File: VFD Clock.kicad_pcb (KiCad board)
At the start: 2 copper layers, 224 x 78.5 mm, 37 parts, among them J2 Mode Button, J3 Up Button, J4 Down Button, J5 Select Button, U1 74HC595, U10 74HC595, U11 UDN2981A, U12 Minute Right, U13 74HC595, U14 UDN2981A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

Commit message: removed all tracks, starting over
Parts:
- moved J5 51.0 mm to (275.5, 143.0)
- moved J4 48.0 mm to (261.5, 143.0)
- moved J3 44.0 mm to (247.5, 143.0)
- moved U21 43.1 mm to (225.4, 126.1)
- moved J2 41.0 mm to (233.5, 143.0)
- moved C10 24.0 mm to (88.5, 119.0)
- moved C1 6.52 mm to (76.0, 92.0)
- moved U13 4.00 mm to (215.5, 114.0)
- moved U5 4.00 mm to (137.5, 84.0)
- moved C8 3.03 mm to (151.0, 119.0)
- moved U7 3.03 mm to (153.5, 114.0)
- moved U4 3.01 mm to (118.5, 114.0)
- moved C9 3.00 mm to (115.0, 119.0)
- moved C7 1.00 mm to (177.0, 119.0)
- moved U10 1.00 mm to (180.5, 114.0)
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- renumbered REF** to Hole1, REF** to Hole2, REF** to Hole3, REF** to Hole4
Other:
- board size 224 x 78.5 mm -> 224 x 78 mm
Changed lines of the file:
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@@
 	(footprint "MountingHole:MountingHole_3.2mm_M3"
 		(layer "F.Cu")
-		(at 66.881135 74.954983)
+		(at 67 75.5)
 		(descr "Mounting Hole 3.2mm, M3, no annular, generated by kicad-footprint-generator mountinghole.py")
 		(tags "mountinghole M3")
-		(property "Reference" "REF**"
+		(property "Reference" "Hole1"
 			(at 0 -4.15 0)
 			(layer "F.SilkS")
@@
 			(layer "F.CrtYd")
 		)
-		(fp_text user "${REFERENCE}"
+		(fp_text user "$Hole1"
 			(at 0 0 0)
 			(layer "F.Fab")
@@
 		(descr "Mounting Hole 3.2mm, M3, no annular, generated by kicad-footprint-generator mountinghole.py")
 		(tags "mountinghole M3")
-		(property "Reference" "REF**"
+		(property "Reference" "Hole4"
 			(at 0 -4.15 0)
 			(layer "F.SilkS")
@@
 			(layer "F.CrtYd")
 		)
-		(fp_text user "${REFERENCE}"
+		(fp_text user "$Hole4"
 			(at 0 0 0)
 			(layer "F.Fab")
@@
 	(footprint "MountingHole:MountingHole_3.2mm_M3"
 		(layer "F.Cu")
-		(at 66.945211 146.450088)
+		(at 67 146.5)
 		(descr "Mounting Hole 3.2mm, M3, no annular, generated by kicad-footprint-generator mountinghole.py")
 		(tags "mountinghole M3")
-		(property "Reference" "REF**"
+		(property "Reference" "Hole2"
 			(at 0 -4.15 0)
 			(layer "F.SilkS")
@@
 			(layer "F.CrtYd")
 		)
-		(fp_text user "${REFERENCE}"
+		(fp_text user "$Hole2"
 			(at 0 0 0)
 			(layer "F.Fab")
@@
 	(footprint "MountingHole:MountingHole_3.2mm_M3"
 		(layer "F.Cu")
-		(at 284 75)
+		(at 284 75.5)
 		(descr "Mounting Hole 3.2mm, M3, no annular, generated by kicad-footprint-generator mountinghole.py")
 		(tags "mountinghole M3")
-		(property "Reference" "REF**"
+		(property "Reference" "Hole3"
 			(at 0 -4.15 0)
 			(layer "F.SilkS")
@@
 			(layer "F.CrtYd")
 		)
-		(fp_text user "${REFERENCE}"
+		(fp_text user "$Hole3"
 			(at 0 0 0)
 			(layer "F.Fab")
@@
 	(footprint "Custom Parts:DS3231 Module"
 		(layer "B.Cu")
-		(at 268.5 126 180)
+		(at 225.4 126.1 180)
 		(property "Reference" "U21"
 			(at 22 -9 0)
@@
 	(footprint "Package_DIP:DIP-16_W7.62mm"
 		(layer "B.Cu")
-		(at 181.5 114 -90)
+		(at 180.5 114 -90)
 		(descr "16-lead though-hole mounted DIP package, row spacing 7.62mm (300 mils)")
 		(tags "THT DIP DIL PDIP 2.54mm 7.62mm 300mil")
@@
 		)
 		(point
-			(at 190.39 117.81)
+			(at 189.39 117.81)
 			(size 1.27)
 			(layer "B.Fab")
@@
 	(footprint "Package_DIP:DIP-16_W7.62mm"
 		(layer "B.Cu")
-		(at 121.5 114.192706 -90)
+		(at 118.5 114 -90)
 		(descr "16-lead though-hole mounted DIP package, row spacing 7.62mm (300 mils)")
 		(tags "THT DIP DIL PDIP 2.54mm 7.62mm 300mil")
@@
 		)
 		(point
-			(at 130.39 118.002706)
+			(at 127.39 117.81)
 			(size 1.27)
 			(layer "B.Fab")
@@
 	(footprint "Capacitor_THT:CP_Radial_D6.3mm_P2.50mm"
 		(layer "B.Cu")
-		(at 69.5 91.44)
+		(at 76 92)
 		(descr "CP, Radial series, Radial, pin pitch=2.50mm, diameter=6.3mm, height=7mm, Electrolytic Capacitor")
 		(tags "CP Radial series Radial pin pitch 2.50mm diameter 6.3mm height 7mm Electrolytic Capacitor")
@@
 	(footprint "Package_DIP:DIP-16_W7.62mm"
 		(layer "B.Cu")
-		(at 211.5 114 -90)
+		(at 215.5 114 -90)
 		(descr "16-lead though-hole mounted DIP package, row spacing 7.62mm (300 mils)")
 		(tags "THT DIP DIL PDIP 2.54mm 7.62mm 300mil")
@@
 		)
 		(point
-			(at 220.39 117.81)
+			(at 224.39 117.81)
 			(size 1.27)
 			(layer "B.Fab")
@@
 	(footprint "Connector_PinHeader_2.54mm:PinHeader_1x02_P2.54mm_Vertical"
 		(layer "B.Cu")
-		(at 192.5 143.5 90)
+		(at 233.5 143 90)
 		(descr "Through hole straight pin header, 1x02, 2.54mm pitch, single row")
 		(tags "Through hole pin header THT 1x02 2.54mm single row")
@@
 	(footprint "Connector_PinHeader_2.54mm:PinHeader_1x02_P2.54mm_Vertical"
 		(layer "B.Cu")
-		(at 224.5 143.5 90)
+		(at 275.5 143 90)
 		(descr "Through hole straight pin header, 1x02, 2.54mm pitch, single row")
 		(tags "Through hole pin header THT 1x02 2.54mm single row")
@@
 	(footprint "Capacitor_THT:C_Disc_D3.0mm_W1.6mm_P2.50mm"
 		(layer "B.Cu")
-		(at 177.997842 118.997706 90)
+		(at 176.997842 118.997706 90)
 		(descr "C, Disc series, Radial, pin pitch=2.50mm, diameter*width=3.0*1.6mm^2, Capacitor, http://www.vishay.com/docs/45233/krseries.pdf")
 		(tags "C Disc series Radial pin pitch 2.50mm diameter 3.0mm width 1.6mm Capacitor")
@@
 	(footprint "UDN2981A:DIP254P762X533-18"
 		(layer "B.Cu")
-		(at 262.5 84 -90)
+		(at 261.5 84 -90)
 		(property "Reference" "U17"
 			(at -3.56197 23.94155 90)
@@
 	(footprint "Connector_PinHeader_2.54mm:PinHeader_1x02_P2.54mm_Vertical"
 		(layer "B.Cu")
-		(at 213.5 143.5 90)
+		(at 261.5 143 90)
 		(descr "Through hole straight pin header, 1x02, 2.54mm pitch, single row")
 		(tags "Through hole pin header THT 1x02 2.54mm single row")
@@
 	(footprint "Capacitor_THT:C_Disc_D3.0mm_W1.6mm_P2.50mm"
 		(layer "B.Cu")
-		(at 147.997842 118.997706 90)
+		(at 151.031186 119.03105 90)
 		(descr "C, Disc series, Radial, pin pitch=2.50mm, diameter*width=3.0*1.6mm^2, Capacitor, http://www.vishay.com/docs/45233/krseries.pdf")
 		(tags "C Disc series Radial pin pitch 2.50mm diameter 3.0mm width 1.6mm Capacitor")
@@
 	(footprint "UDN2981A:DIP254P762X533-18"
 		(layer "B.Cu")
-		(at 141.5 84 -90)
+		(at 137.5 84 -90)
 		(property "Reference" "U5"
 			(at -3.56197 23.94155 90)
@@
 	(footprint "Package_DIP:DIP-16_W7.62mm"
 		(layer "B.Cu")
-		(at 242.5 114 -90)
+		(at 242.72 114 -90)
 		(descr "16-lead though-hole mounted DIP package, row spacing 7.62mm (300 mils)")
 		(tags "THT DIP DIL PDIP 2.54mm 7.62mm 300mil")
@@
 		)
 		(point
-			(at 251.39 117.81)
+			(at 251.61 117.81)
 			(size 1.27)
 			(layer "B.Fab")
@@
 	(footprint "Connector_PinHeader_2.54mm:PinHeader_1x02_P2.54mm_Vertical"
 		(layer "B.Cu")
-		(at 203.5 143.5 90)
+		(at 247.5 143 90)
 		(descr "Through hole straight pin header, 1x02, 2.54mm pitch, single row")
 		(tags "Through hole pin header THT 1x02 2.54mm single row")
@@
 	(footprint "Capacitor_THT:C_Disc_D3.0mm_W1.6mm_P2.50mm"
 		(layer "B.Cu")
-		(at 117.997842 118.997706 90)
+		(at 114.997842 118.997706 90)
 		(descr "C, Disc series, Radial, pin pitch=2.50mm, diameter*width=3.0*1.6mm^2, Capacitor, http://www.vishay.com/docs/45233/krseries.pdf")
 		(tags "C Disc series Radial pin pitch 2.50mm diameter 3.0mm width 1.6mm Capacitor")
@@
 	(footprint "Capacitor_THT:C_Disc_D3.0mm_W1.6mm_P2.50mm"
 		(layer "B.Cu")
-		(at 112.5 119 90)
+		(at 88.5 119 90)
 		(descr "C, Disc series, Radial, pin pitch=2.50mm, diameter*width=3.0*1.6mm^2, Capacitor, http://www.vishay.com/docs/45233/krseries.pdf")
 		(tags "C Disc series Radial pin pitch 2.50mm diameter 3.0mm width 1.6mm Capacitor")
@@
 	(footprint "Package_DIP:DIP-16_W7.62mm"
 		(layer "B.Cu")
-		(at 150.5 114 -90)
+		(at 153.533344 114 -90)
 		(descr "16-lead though-hole mounted DIP package, row spacing 7.62mm (300 mils)")
 		(tags "THT DIP DIL PDIP 2.54mm 7.62mm 300mil")
@@
 		)
 		(point
-			(at 159.39 117.81)
+			(at 162.423344 117.81)
 			(size 1.27)
 			(layer "B.Fab")
@@
 	)
 	(gr_rect
-		(start 63.5 71.75)
-		(end 287.5 150.25)
+		(start 63.5 72)
+		(end 287.5 150)
 		(stroke
 			(width 0.05)
@@
 	)
 	(gr_text "IV-11 VFD Tube Clock\nMade in Wisconsin\nAron Szucs 2026\n"
-		(at 276.5 81 270)
+		(at 293.5 81.5 270)
 		(layer "F.SilkS")
 		(effects

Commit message: save
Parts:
- moved C11 4.61 mm to (212.5, 120.0)
- moved C8 1.13 mm to (150.5, 120.0)
- moved C12 1.12 mm to (239.5, 120.0)
- moved C7 1.12 mm to (177.5, 120.0)
- moved C9 1.12 mm to (115.5, 120.0)
- moved C10 1.00 mm to (88.5, 120.0)
- moved U1 1.00 mm to (91.5, 115.0)
- moved U10 1.00 mm to (180.5, 115.0)
- moved U13 1.00 mm to (215.5, 115.0)
- moved U16 1.00 mm to (242.7, 115.0)
- moved U20 1.00 mm to (137.5, 125.5)
- moved U4 1.00 mm to (118.5, 115.0)
- moved U7 1.00 mm to (153.5, 115.0)
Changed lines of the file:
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@@
 	)
 	(setup
+		(stackup
+			(layer "F.SilkS"
+				(type "Top Silk Screen")
+			)
+			(layer "F.Paste"
+				(type "Top Solder Paste")
+			)
+			(layer "F.Mask"
+				(type "Top Solder Mask")
+				(thickness 0.01)
+			)
+			(layer "F.Cu"
+				(type "copper")
+				(thickness 0.035)
+			)
+			(layer "dielectric 1"
+				(type "core")
+				(thickness 1.51)
+				(material "FR4")
+				(epsilon_r 4.5)
+				(loss_tangent 0.02)
+			)
+			(layer "B.Cu"
+				(type "copper")
+				(thickness 0.035)
+			)
+			(layer "B.Mask"
+				(type "Bottom Solder Mask")
+				(thickness 0.01)
+			)
+			(layer "B.Paste"
+				(type "Bottom Solder Paste")
+			)
+			(layer "B.SilkS"
+				(type "Bottom Silk Screen")
+			)
+			(copper_finish "None")
+			(dielectric_constraints no)
+		)
 		(pad_to_mask_clearance 0)
 		(allow_soldermask_bridges_in_footprints no)
@@
 		(capping no)
 		(filling no)
+		(zone_defaults)
 		(grid_origin 175.5 100)
 		(pcbplotparams
@@
 	(footprint "Package_DIP:DIP-16_W7.62mm"
 		(layer "B.Cu")
-		(at 180.5 114 -90)
+		(at 180.5 115 -90)
 		(descr "16-lead though-hole mounted DIP package, row spacing 7.62mm (300 mils)")
 		(tags "THT DIP DIL PDIP 2.54mm 7.62mm 300mil")
@@
 		)
 		(point
-			(at 189.39 117.81)
+			(at 189.39 118.81)
 			(size 1.27)
 			(layer "B.Fab")
@@
 	(footprint "Package_DIP:DIP-16_W7.62mm"
 		(layer "B.Cu")
-		(at 118.5 114 -90)
+		(at 118.5 115 -90)
 		(descr "16-lead though-hole mounted DIP package, row spacing 7.62mm (300 mils)")
 		(tags "THT DIP DIL PDIP 2.54mm 7.62mm 300mil")
@@
 		)
 		(point
-			(at 127.39 117.81)
+			(at 127.39 118.81)
 			(size 1.27)
 			(layer "B.Fab")
@@
 	(footprint "Package_DIP:DIP-16_W7.62mm"
 		(layer "B.Cu")
-		(at 215.5 114 -90)
+		(at 215.5 115 -90)
 		(descr "16-lead though-hole mounted DIP package, row spacing 7.62mm (300 mils)")
 		(tags "THT DIP DIL PDIP 2.54mm 7.62mm 300mil")
@@
 		)
 		(point
-			(at 224.39 117.81)
+			(at 224.39 118.81)
 			(size 1.27)
 			(layer "B.Fab")
@@
 	(footprint "Package_DIP:DIP-16_W7.62mm"
 		(layer "B.Cu")
-		(at 91.5 114 -90)
+		(at 91.5 115 -90)
 		(descr "16-lead though-hole mounted DIP package, row spacing 7.62mm (300 mils)")
 		(tags "THT DIP DIL PDIP 2.54mm 7.62mm 300mil")
@@
 		)
 		(point
-			(at 100.39 117.81)
+			(at 100.39 118.81)
 			(size 1.27)
 			(layer "B.Fab")
@@
 	(footprint "Capacitor_THT:C_Disc_D3.0mm_W1.6mm_P2.50mm"
 		(layer "B.Cu")
-		(at 176.997842 118.997706 90)
+		(at 177.5 119.997706 90)
 		(descr "C, Disc series, Radial, pin pitch=2.50mm, diameter*width=3.0*1.6mm^2, Capacitor, http://www.vishay.com/docs/45233/krseries.pdf")
 		(tags "C Disc series Radial pin pitch 2.50mm diameter 3.0mm width 1.6mm Capacitor")
@@
 	(footprint "Custom Parts:LM2596 Module"
 		(layer "B.Cu")
-		(at 137.5 124.5047 180)
+		(at 137.5 125.5047 180)
 		(property "Reference" "U20"
 			(at 25.4 -8.66 0)
@@
 	(footprint "Capacitor_THT:C_Disc_D3.0mm_W1.6mm_P2.50mm"
 		(layer "B.Cu")
-		(at 151.031186 119.03105 90)
+		(at 150.5 120.03105 90)
 		(descr "C, Disc series, Radial, pin pitch=2.50mm, diameter*width=3.0*1.6mm^2, Capacitor, http://www.vishay.com/docs/45233/krseries.pdf")
 		(tags "C Disc series Radial pin pitch 2.50mm diameter 3.0mm width 1.6mm Capacitor")
@@
 	(footprint "Capacitor_THT:C_Disc_D3.0mm_W1.6mm_P2.50mm"
 		(layer "B.Cu")
-		(at 207.997842 118.997706 90)
+		(at 212.5 119.997706 90)
 		(descr "C, Disc series, Radial, pin pitch=2.50mm, diameter*width=3.0*1.6mm^2, Capacitor, http://www.vishay.com/docs/45233/krseries.pdf")
 		(tags "C Disc series Radial pin pitch 2.50mm diameter 3.0mm width 1.6mm Capacitor")
@@
 	(footprint "Capacitor_THT:C_Disc_D3.0mm_W1.6mm_P2.50mm"
 		(layer "B.Cu")
-		(at 238.997842 118.997706 90)
+		(at 239.5 119.997706 90)
 		(descr "C, Disc series, Radial, pin pitch=2.50mm, diameter*width=3.0*1.6mm^2, Capacitor, http://www.vishay.com/docs/45233/krseries.pdf")
 		(tags "C Disc series Radial pin pitch 2.50mm diameter 3.0mm width 1.6mm Capacitor")
@@
 	(footprint "Package_DIP:DIP-16_W7.62mm"
 		(layer "B.Cu")
-		(at 242.72 114 -90)
+		(at 242.72 115 -90)
 		(descr "16-lead though-hole mounted DIP package, row spacing 7.62mm (300 mils)")
 		(tags "THT DIP DIL PDIP 2.54mm 7.62mm 300mil")
@@
 		)
 		(point
-			(at 251.61 117.81)
+			(at 251.61 118.81)
 			(size 1.27)
 			(layer "B.Fab")
@@
 	(footprint "Capacitor_THT:C_Disc_D3.0mm_W1.6mm_P2.50mm"
 		(layer "B.Cu")
-		(at 114.997842 118.997706 90)
+		(at 115.5 119.997706 90)
 		(descr "C, Disc series, Radial, pin pitch=2.50mm, diameter*width=3.0*1.6mm^2, Capacitor, http://www.vishay.com/docs/45233/krseries.pdf")
 		(tags "C Disc series Radial pin pitch 2.50mm diameter 3.0mm width 1.6mm Capacitor")
@@
 	(footprint "Capacitor_THT:C_Disc_D3.0mm_W1.6mm_P2.50mm"
 		(layer "B.Cu")
-		(at 88.5 119 90)
+		(at 88.5 120 90)
 		(descr "C, Disc series, Radial, pin pitch=2.50mm, diameter*width=3.0*1.6mm^2, Capacitor, http://www.vishay.com/docs/45233/krseries.pdf")
 		(tags "C Disc series Radial pin pitch 2.50mm diameter 3.0mm width 1.6mm Capacitor")
@@
 		)
 		(property "Value" "100nF"
-			(at 5 1 180)
+			(at 6 0 90)
 			(layer "B.SilkS")
 			(effects
@@
 	(footprint "Package_DIP:DIP-16_W7.62mm"
 		(layer "B.Cu")
-		(at 153.533344 114 -90)
+		(at 153.533344 115 -90)
 		(descr "16-lead though-hole mounted DIP package, row spacing 7.62mm (300 mils)")
 		(tags "THT DIP DIL PDIP 2.54mm 7.62mm 300mil")
@@
 		)
 		(point
-			(at 162.423344 117.81)
+			(at 162.423344 118.81)
 			(size 1.27)
 			(layer "B.Fab")
@@
 	)
 	(gr_text "IV-11 VFD Tube Clock\nMade in Wisconsin\nAron Szucs 2026\n"
-		(at 293.5 81.5 270)
+		(at 276.5 80 270)
 		(layer "F.SilkS")
 		(effects

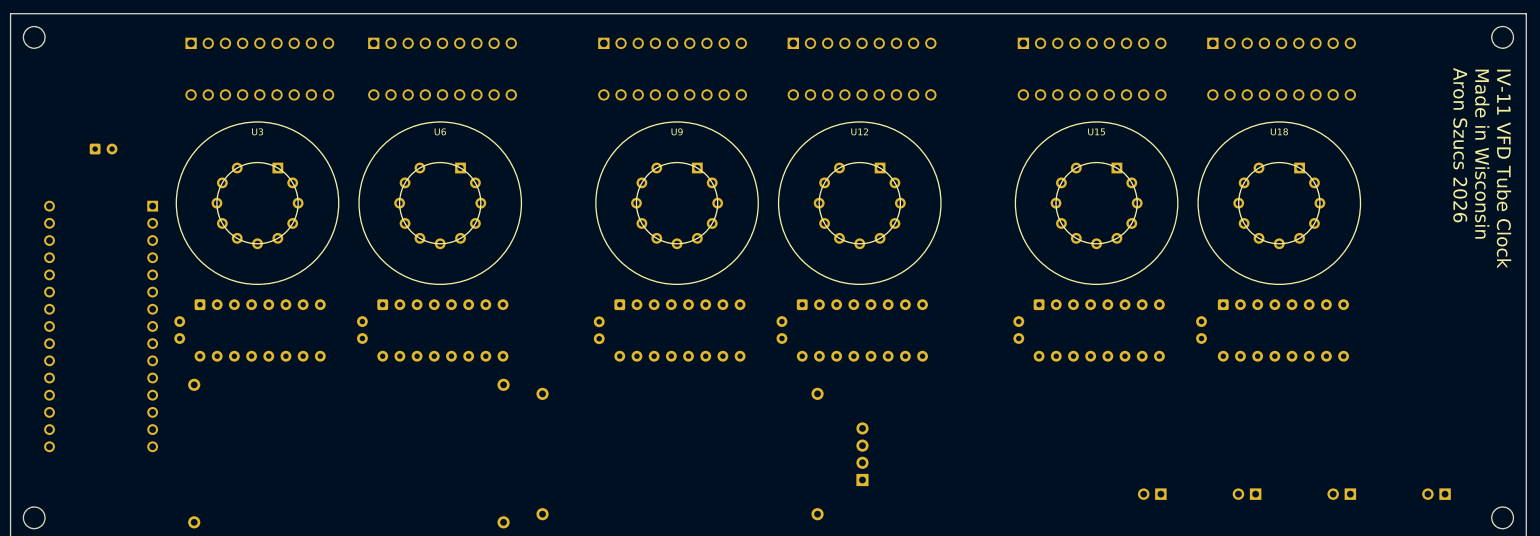
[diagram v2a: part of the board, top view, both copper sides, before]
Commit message: add debouncing caps
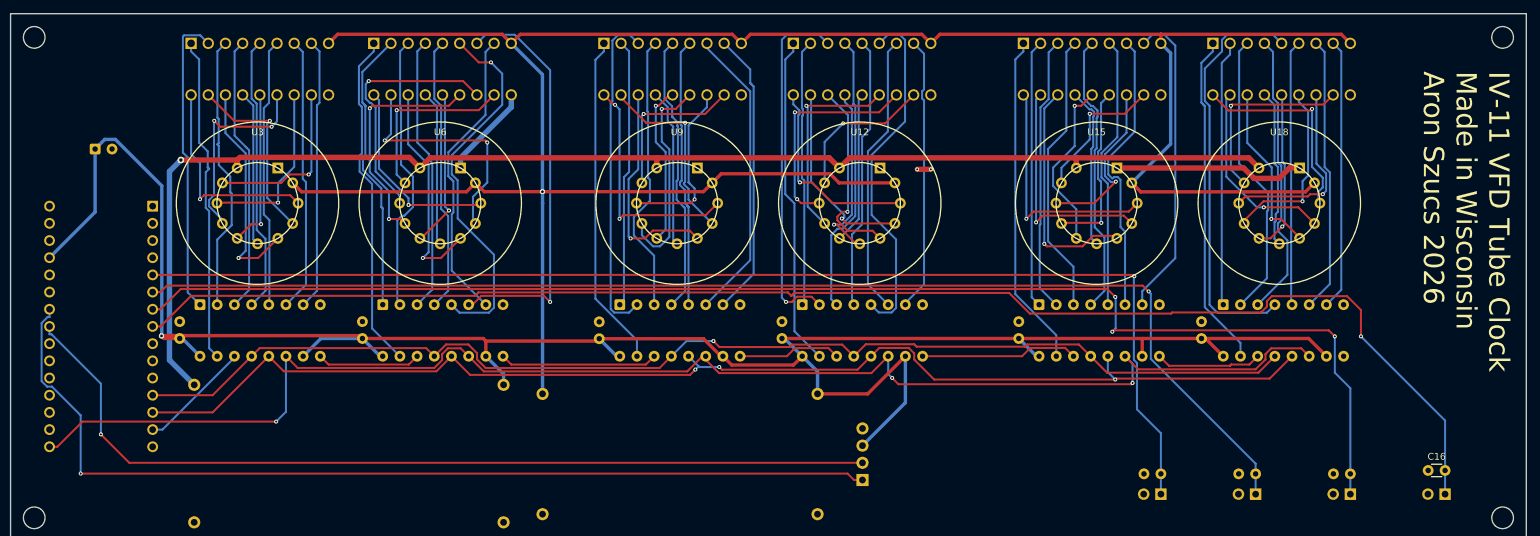
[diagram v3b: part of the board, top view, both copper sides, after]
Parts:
- added C13: 100nF, Capacitor_THT:C_Disc_D3.0mm_W1.6mm_P2.50mm, B.Cu at (231.0, 140.0)
- added C14: 100nF, Capacitor_THT:C_Disc_D3.0mm_W1.6mm_P2.50mm, B.Cu at (245.0, 140.0)
- added C15: 100nF, Capacitor_THT:C_Disc_D3.0mm_W1.6mm_P2.50mm, B.Cu at (259.0, 140.0)
- added C16: 100nF, Capacitor_THT:C_Disc_D3.0mm_W1.6mm_P2.50mm, F.Cu at (273.0, 139.5)
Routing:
- net +25V: track 0.00 -> 354.5 mm, vias 0 -> 1
- net +5V: track 0.00 -> 318.2 mm, vias 0 -> 1
- net /Select_Button: track 0.00 -> 217.6 mm, vias 0 -> 1
- net /Shift: track 0.00 -> 215.5 mm, vias 0 -> 3
- net /Down_Button: track 0.00 -> 206.9 mm, vias 0 -> 3
- net +1.5V: track 0.00 -> 202.2 mm, vias 0 -> 1
- net /Latch: track 0.00 -> 186.8 mm, vias 0 -> 3
- net /Up_Button: track 0.00 -> 184.4 mm, vias 0 -> 1
- net /Mode_Button: track 0.00 -> 179.0 mm, vias 0 -> 1
- net /OE_PWM: track 0.00 -> 178.5 mm, vias 0 -> 1
- net /SCL: track 0.00 -> 143.7 mm, vias 0 -> 1
- net /SDA: track 0.00 -> 133.6 mm, vias 0 -> 1
- net Net-(U16-QE): track 0.00 -> 60.8 mm
- net Net-(U4-QG): track 0.00 -> 60.7 mm, vias 0 -> 1
- net Net-(U4-QF): track 0.00 -> 55.5 mm, vias 0 -> 1
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
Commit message: checkpoint
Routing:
- net Net-(U10-QF): track 52.2 -> 47.8 mm, vias 0 -> 2
- net GND: track 44.2 -> 42.2 mm, vias 2 -> 0

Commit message: GND pour
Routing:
- net GND: track 42.2 -> 28.3 mm
- added copper zone on B.Cu, net GND
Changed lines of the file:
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@@
 	)
 	(segment
-		(start 137.5 85.8021)
-		(end 137.5 84)
-		(width 0.8)
-		(layer "B.Cu")
-		(net "GND")
-	)
-	(segment
-		(start 130 94.8038)
-		(end 130 93.3021)
-		(width 0.8)
-		(layer "B.Cu")
-		(net "GND")
-	)
-	(segment
-		(start 130 93.3021)
-		(end 137.5 85.8021)
-		(width 0.8)
-		(layer "B.Cu")
-		(net "GND")
-	)
-	(segment
 		(start 185.95 97)
 		(end 184.6024 95.6524)
@@
 		(net "Net-(U7-QH)")
 	)
+	(zone
+		(net "GND")
+		(layer "B.Cu")
+		(name "Ground Pour")
+		(hatch none 0.5)
+		(connect_pads
+			(clearance 0.25)
+		)
+		(min_thickness 0.25)
+		(fill yes
+			(thermal_gap 0.4)
+			(thermal_bridge_width 0.25)
+			(smoothing fillet)
+			(radius 0.5)
+			(island_removal_mode 0)
+		)
+		(polygon
+			(pts
+				(xy 63.5 72) (xy 63.5 150) (xy 287.5 150) (xy 287.5 72)
+			)
+		)
+	)
 	(embedded_fonts no)

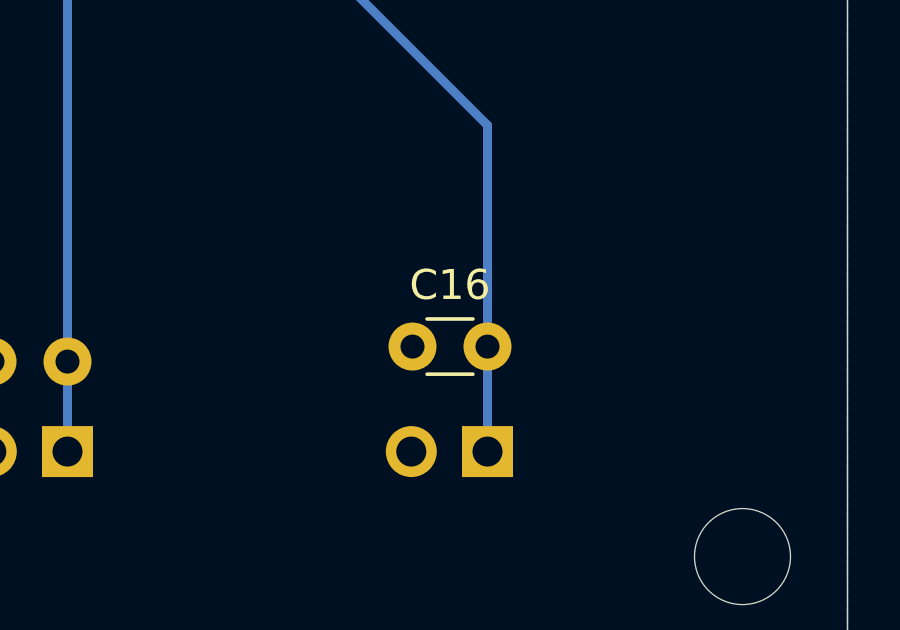
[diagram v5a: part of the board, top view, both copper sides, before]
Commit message: IV-11 Tube footprint was flipped, unflipped it
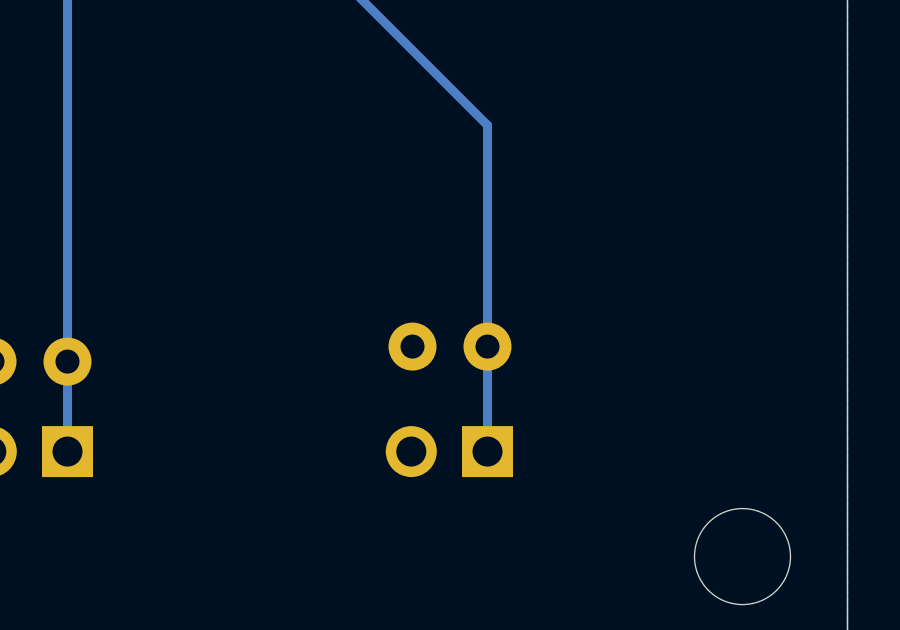
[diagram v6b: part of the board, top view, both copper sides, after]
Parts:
- C16: moved to B.Cu
